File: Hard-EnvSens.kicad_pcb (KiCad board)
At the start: 2 copper layers, 54 parts, among them Q1 SS8050, Q2 SS8050, U1 LD1117S33TR_SOT223, U2 ESP32-C6-WROOM-1, U3 CP2104, U4 VEML7700-TR, U5 DPS368, U6 SGP41-D-R4, U7 SHT40-AD1B-R2

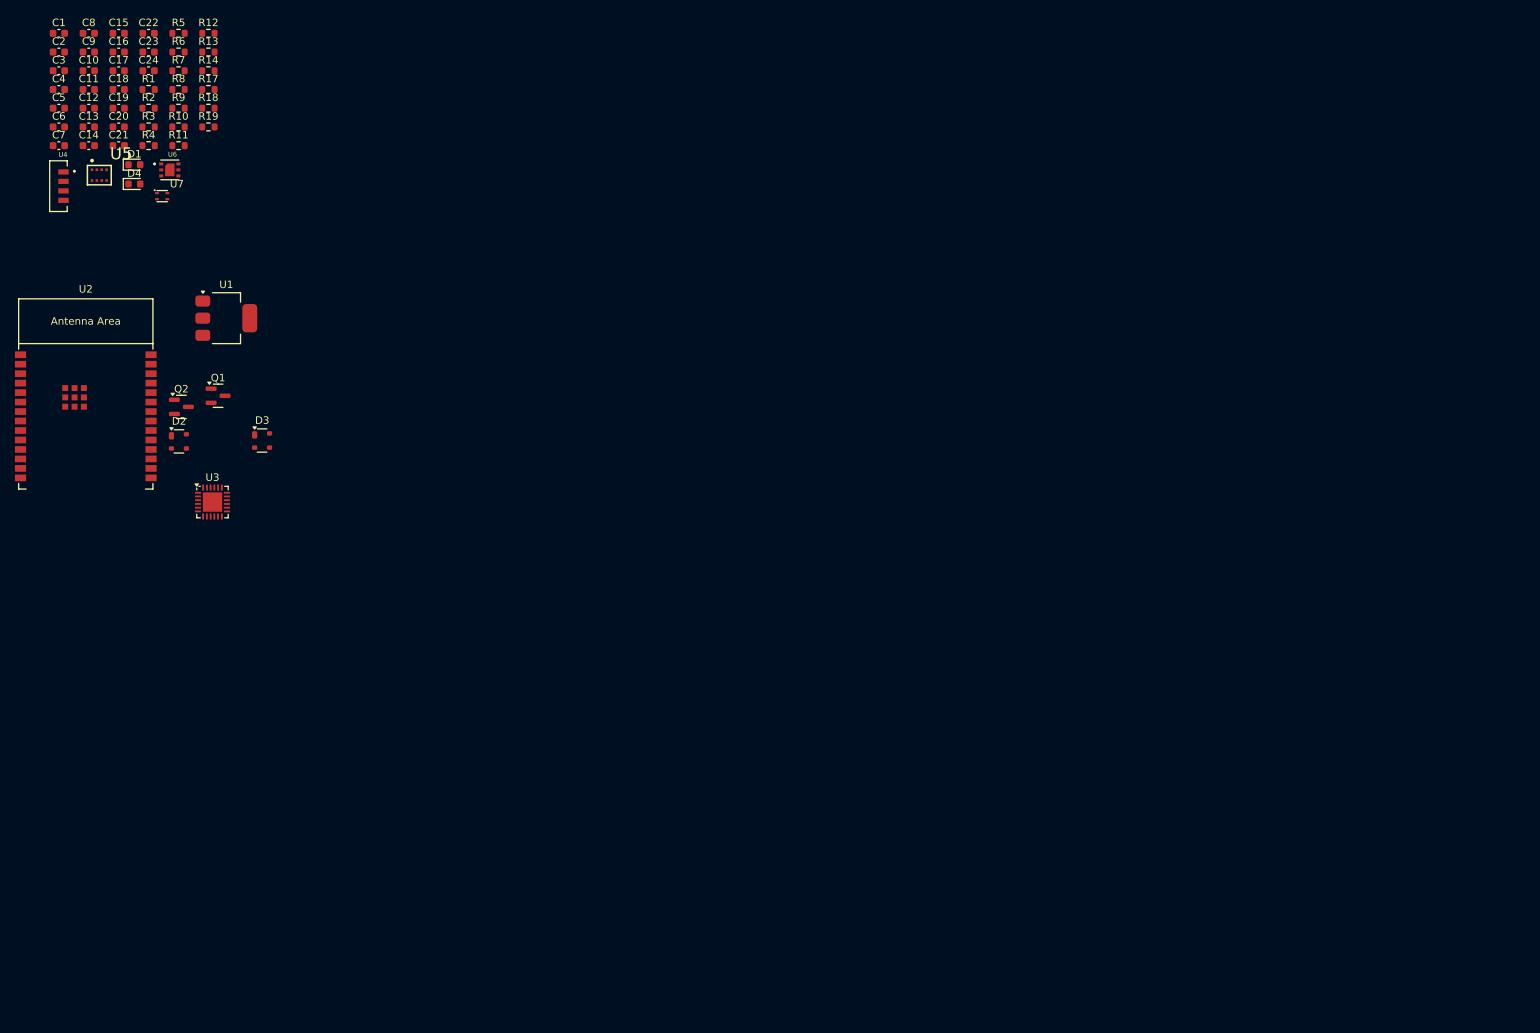
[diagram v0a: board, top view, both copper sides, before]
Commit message: Schematic done, Bottom board
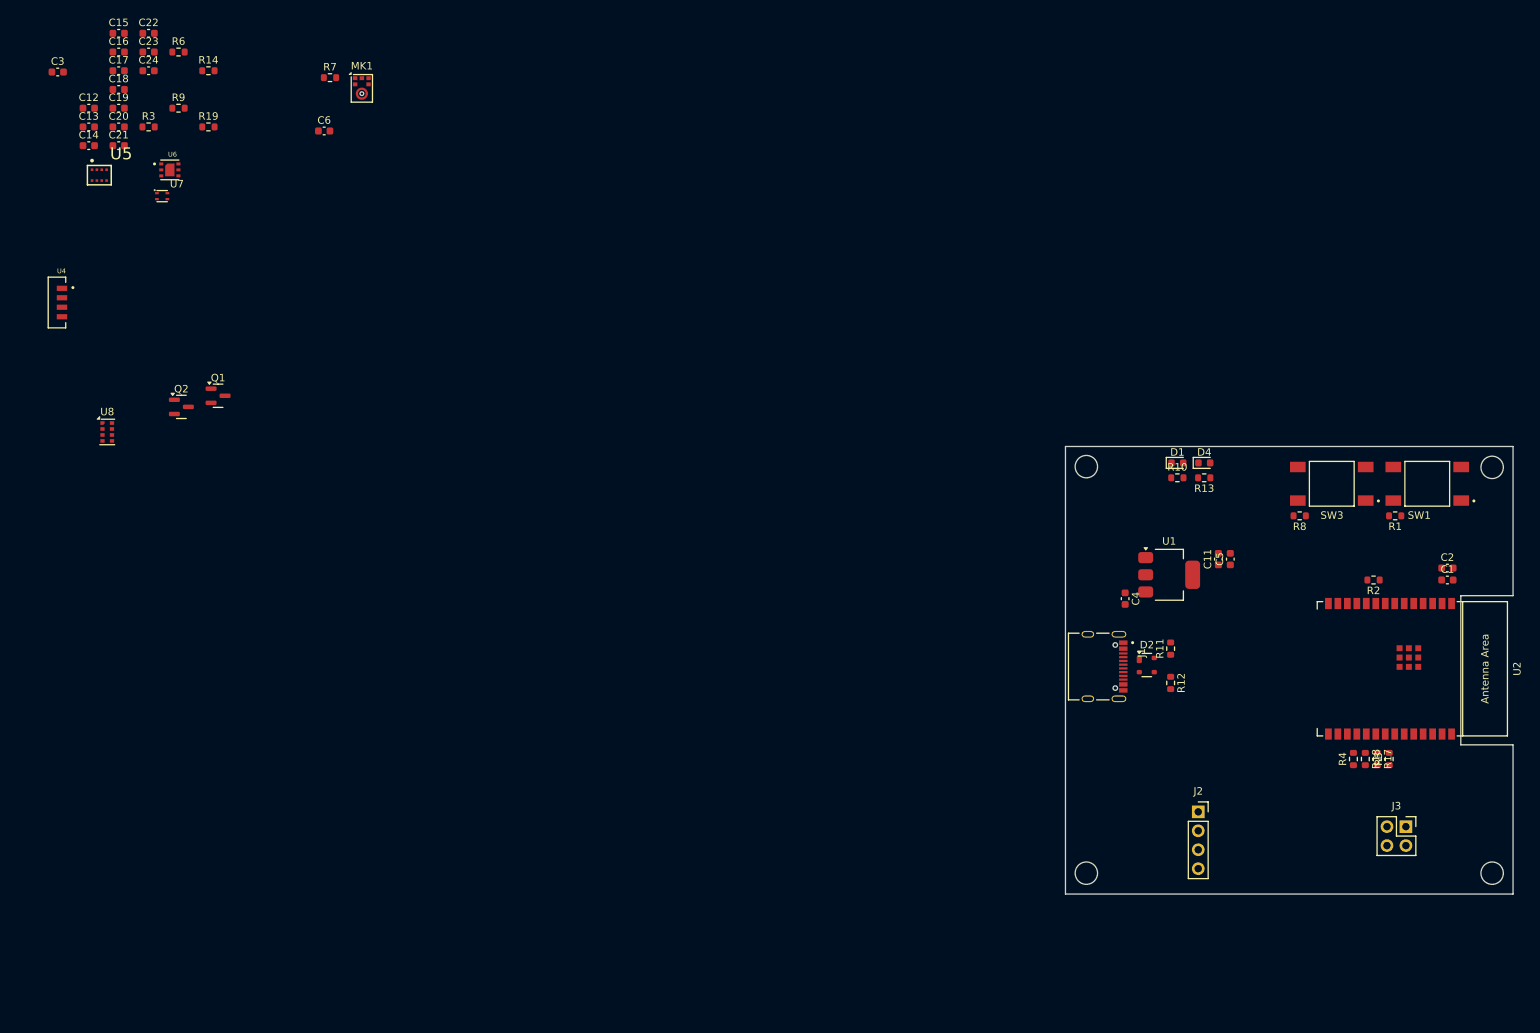
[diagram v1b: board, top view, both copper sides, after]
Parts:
- removed C10: 4.7k, Capacitor_SMD:C_0603_1608Metric
- removed C7, C8: 100nF, Capacitor_SMD:C_0603_1608Metric
- removed C9: 10uF, Capacitor_SMD:C_0603_1608Metric
- removed D3: SP0503BAHT, Package_TO_SOT_SMD:SOT-143
- removed U3: CP2104, Package_DFN_QFN:QFN-24-1EP_4x4mm_P0.5mm_EP2.6x2.6mm
- added J1: TYPE-C-31-M-12, Biblioteca_Kicad:HRO_TYPE-C-31-M-12, F.Cu at (103.1, 79.7)
- added J2: Conn_01x04_Socket, Connector_PinSocket_2.54mm:PinSocket_1x04_P2.54mm_Vertical, F.Cu at (117.9, 99.2)
- added J3: Conn_02x02_Odd_Even, Connector_PinSocket_2.54mm:PinSocket_2x02_P2.54mm_Vertical, F.Cu at (145.7, 101.2)
- added MK1: ICS-43434, Sensor_Audio:InvenSense_ICS-43434-6_3.5x2.65mm, F.Cu at (5.78, 2.19)
- added SW1: SW_Push, Biblioteca_Kicad:SW_3-1437565-0, F.Cu at (148.6, 55.2)
- added SW3: SW_Push, Biblioteca_Kicad:SW_3-1437565-0, F.Cu at (135.8, 55.2)
- added U8: AS7341-DLGT, Package_LGA:AMS_OLGA-8_2x3.1mm_P0.8mm, F.Cu at (-28.4, 48.3)
- C6: value 10uF -> 4.7uF
- R11, R12: value 100R -> 5.11k
- R7: value 4.7k -> 100K
- moved C1 200.1 mm to (151.3, 68.1)
- moved C2 198.6 mm to (151.3, 66.5)
- moved R5 189.2 mm to (143.5, 92.1), turned to 90 degrees
- moved R4 181.2 mm to (138.7, 92.1), turned to 90 degrees
- moved R17 180.6 mm to (141.9, 92.1), turned to -90 degrees
- moved U2 178.1 mm to (143.6, 80.0), turned to -90 degrees
- moved R18 178.0 mm to (140.3, 92.1), turned to -90 degrees
- moved R1 176.6 mm to (144.3, 59.5), turned to 180 degrees
- moved R2 176.0 mm to (141.4, 68.1), turned to 180 degrees
- moved C5 168.3 mm to (122.2, 65.3), turned to 90 degrees
- moved C11 164.0 mm to (120.6, 65.3), turned to 90 degrees
- moved R8 160.8 mm to (131.5, 59.5), turned to 180 degrees
- moved C4 158.4 mm to (108.1, 70.6), turned to -90 degrees
- moved R12 155.6 mm to (114.2, 81.9), turned to -90 degrees
- moved R11 149.1 mm to (114.2, 77.3), turned to 90 degrees
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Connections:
- C20 pad 1: +5V -> +3V3
- D2 pad 2: Net-(P1-D+) -> D+
- D2 pad 3: Net-(P1-D-) -> D-
- R11 pad 2: TX -> GND
- R12 pad 2: RX -> GND
- R7 pad 1: Net-(U3-~{RST}) -> GND
- R7 pad 2: +3V3 -> SD
- U2 pad 5: unconnected-(U2-MTDI/GPIO5/ADC1_CH5-Pad5) -> SD
- U2 pad 6: unconnected-(U2-MTCK/GPIO6/ADC1_CH6-Pad6) -> SCK
- U2 pad 7: unconnected-(U2-MTDO/GPIO7-Pad7) -> WS
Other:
- board outline added: 60 x 60 mm

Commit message: Started connections and sensors pcb
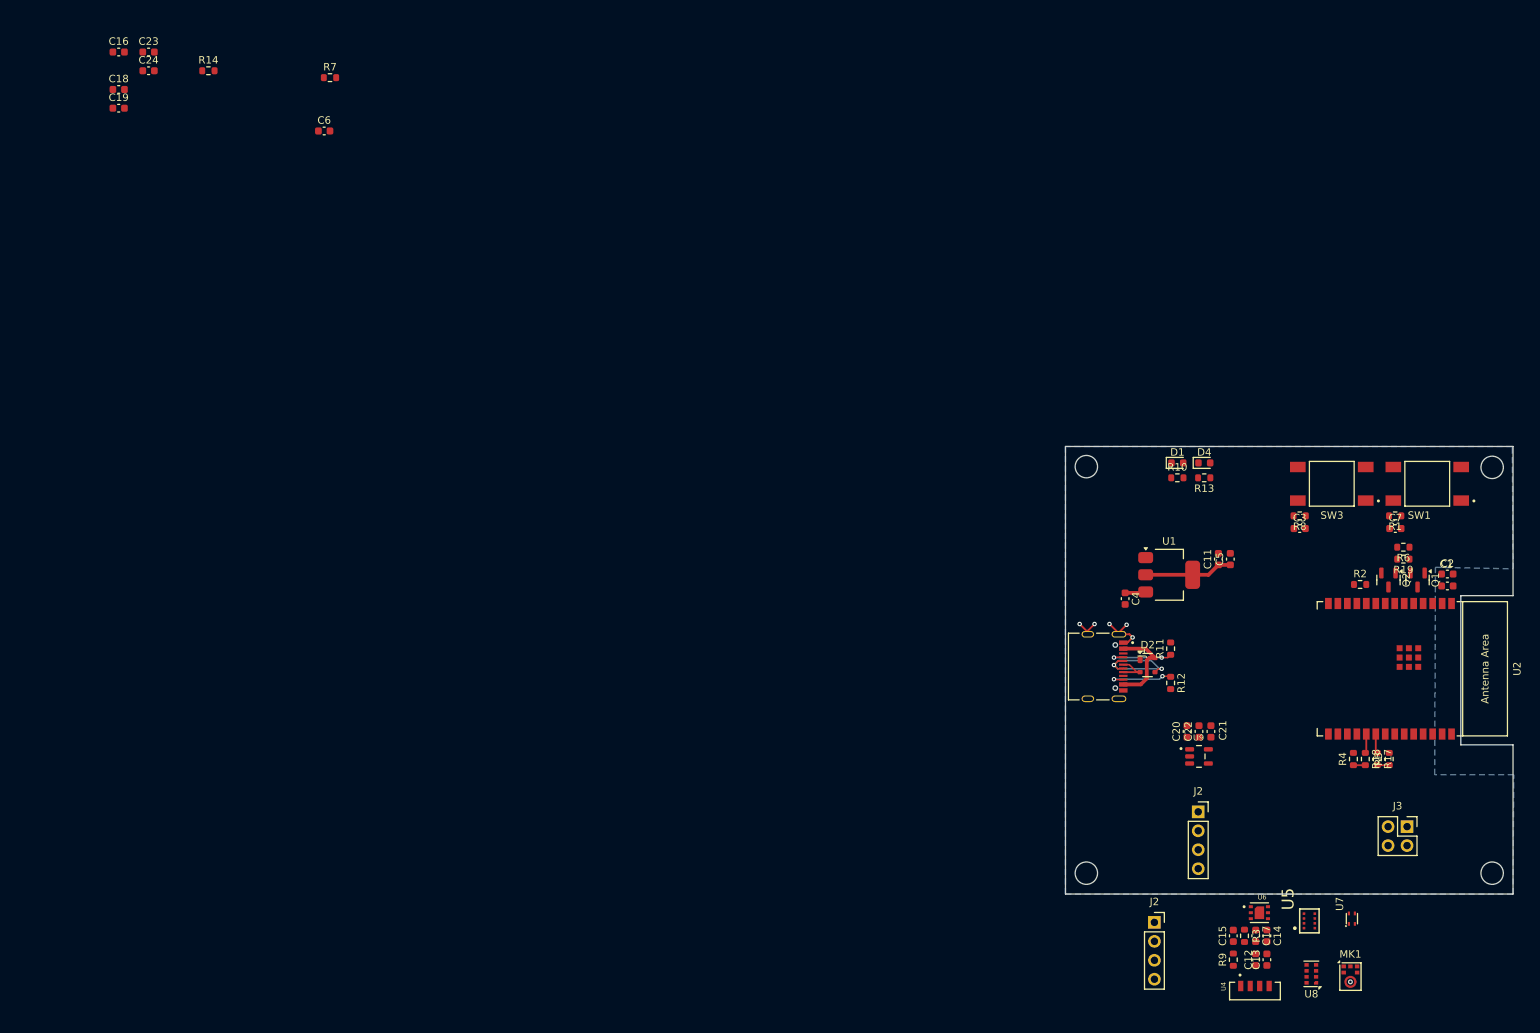
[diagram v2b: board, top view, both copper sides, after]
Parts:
- added C7: 1uF, Capacitor_SMD:C_0603_1608Metric, F.Cu at (144.3, 61.2)
- added J2: Conn_01x04_Socket, Connector_PinSocket_2.54mm:PinSocket_1x04_P2.54mm_Vertical, F.Cu at (112.0, 114.0)
- added U9: TPS79318DBVTG4, libs:SOT95P280X145-5N, F.Cu at (118.0, 91.8)
- moved C12 193.7 mm to (125.6, 119.0), turned to 90 degrees
- moved C13 193.4 mm to (127.1, 119.0), turned to 90 degrees
- moved C15 192.3 mm to (122.6, 115.8), turned to 90 degrees
- moved C17 191.5 mm to (125.6, 115.8), turned to -90 degrees
- moved U5 190.6 mm to (132.8, 113.8), turned to 90 degrees
- moved C14 190.2 mm to (127.1, 115.8), turned to -90 degrees
- moved U7 186.6 mm to (138.5, 113.5), turned to 90 degrees
- moved U4 185.2 mm to (125.5, 123.2), turned to 90 degrees
- moved R3 182.6 mm to (124.1, 115.8), turned to -90 degrees
- moved R9 181.7 mm to (122.6, 119.0), turned to 90 degrees
- moved MK1 178.2 mm to (138.3, 121.3)
- moved C3 177.4 mm to (131.5, 61.2)
- moved R6 177.1 mm to (145.4, 63.7), turned to 180 degrees
- moved U8 177.0 mm to (133.1, 120.9), turned to 180 degrees
- moved U6 176.8 mm to (126.1, 112.7)
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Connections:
- U2 pad 15: IO9 -> unconnected-(U2-GPIO9-Pad15)
- U2 pad 4: unconnected-(U2-MTMS/GPIO4/ADC1_CH4-Pad4) -> IO9
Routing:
- net D-: track 0.00 -> 17.8 mm, vias 0 -> 2
- net +5V: track 0.00 -> 14.7 mm
- net +3V3: track 0.00 -> 11.9 mm
- net GND: track 0.00 -> 10.7 mm, vias 0 -> 5
- net Net-(J1-CC2): track 0.00 -> 9.07 mm, vias 0 -> 2
- net Net-(J1-CC1): track 0.00 -> 9.03 mm, vias 0 -> 2
- net D+: track 0.00 -> 5.04 mm
- net Net-(U2-GPIO22): track 0.00 -> 2.61 mm
- net Net-(U2-GPIO21): track 0.00 -> 2.58 mm
- net Sda: track 0.00 -> 1.60 mm
- net Scl: track 0.00 -> 1.60 mm
- added copper zone on B.Cu, net GND

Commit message: Full connected board, no charger
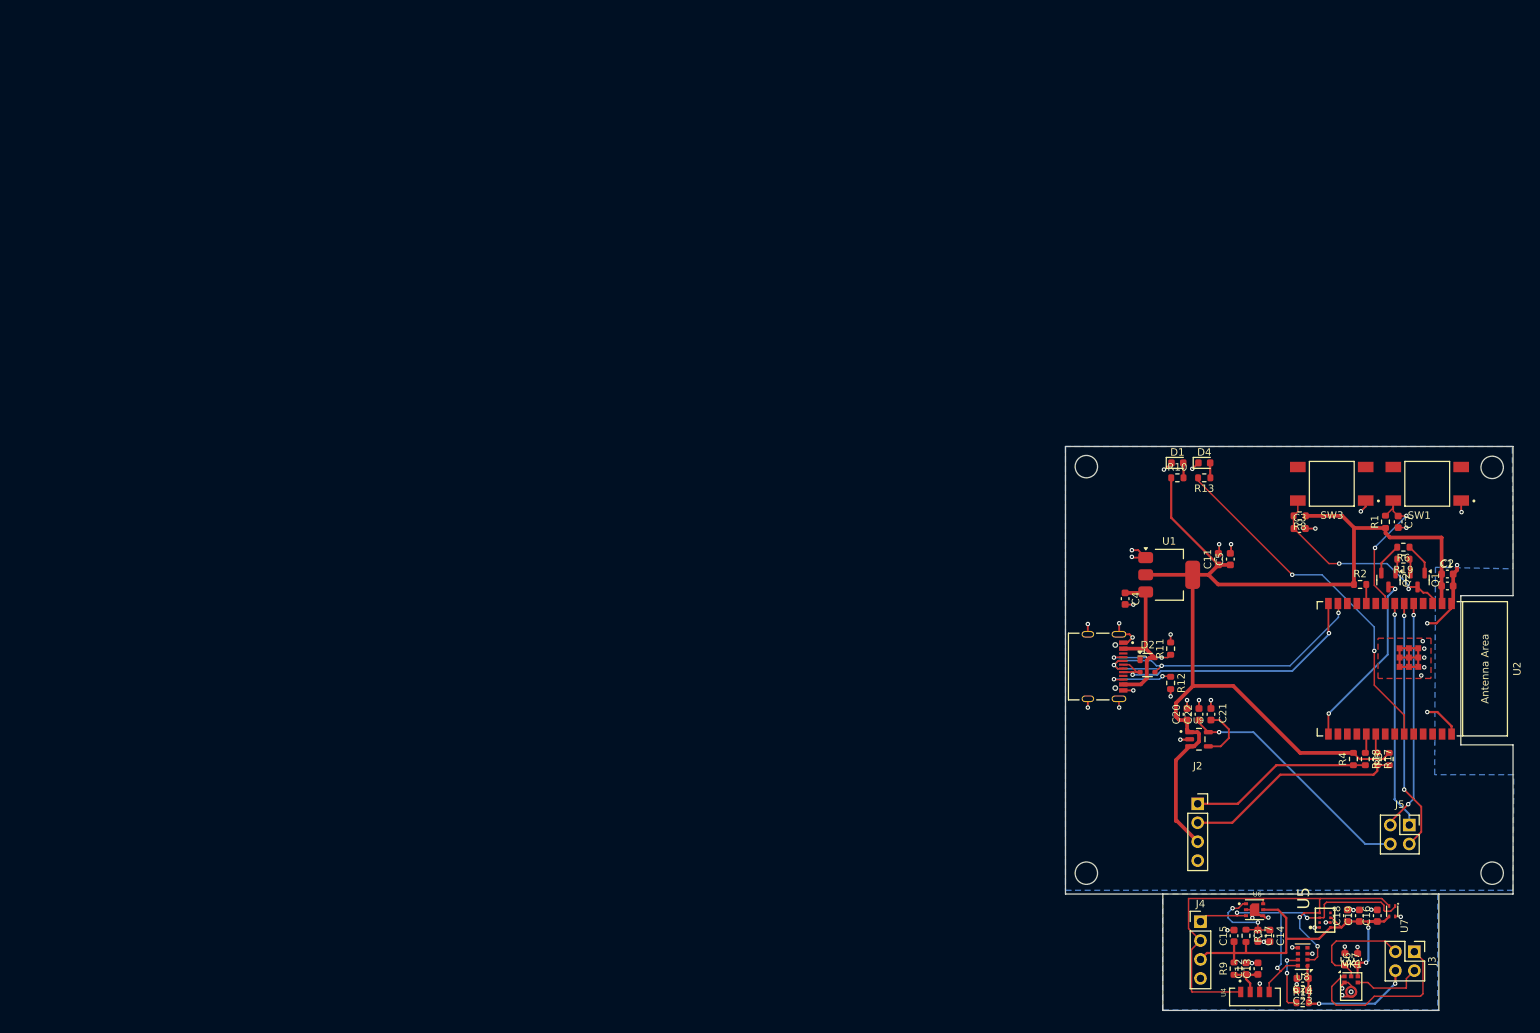
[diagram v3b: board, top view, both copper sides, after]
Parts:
- removed the J2 at (112.0, 114.0)
- added J4: Conn_01x04_Pin, Connector_PinHeader_2.54mm:PinHeader_1x04_P2.54mm_Vertical, F.Cu at (118.2, 113.9)
- added J5: Conn_02x02_Odd_Even, Connector_PinSocket_2.54mm:PinSocket_2x02_P2.54mm_Vertical, F.Cu at (146.2, 101.0)
- C12: value C_Small -> 100nF
- C13: value C_Small -> 10uF
- J3: footprint Connector_PinSocket_2.54mm:PinSocket_2x02_P2.54mm_Vertical -> Connector_PinHeader_2.54mm:PinHeader_2x02_P2.54mm_Vertical
- moved C16 204.6 mm to (141.9, 113.1), turned to 90 degrees
- moved C23 199.4 mm to (131.9, 123.1), turned to 180 degrees
- moved C18 198.5 mm to (137.9, 113.1), turned to 90 degrees
- moved C19 198.4 mm to (139.5, 113.1), turned to 90 degrees
- moved C24 196.8 mm to (131.9, 121.5), turned to 180 degrees
- moved R14 192.7 mm to (131.9, 124.8)
- moved R7 180.2 mm to (137.6, 119.0), turned to -90 degrees
- moved C6 177.6 mm to (139.3, 119.0), turned to 90 degrees
- moved J3 16.8 mm to (146.9, 117.9), turned to -90 degrees
- moved U7 5.49 mm to (143.9, 112.5), turned to -90 degrees
- moved U8 2.58 mm to (131.9, 118.6)
- moved C20 2.30 mm to (116.4, 86.1)
- moved C21 2.30 mm to (119.6, 86.1)
- moved C22 2.30 mm to (118.0, 86.1)
- moved U9 2.30 mm to (118.0, 89.5)
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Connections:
- C12 pad 2: GND -> GND2
- C13 pad 2: GND -> GND2
- C14 pad 2: GND -> GND2
- C15 pad 1: +3V3 -> +3V3top
- C15 pad 2: GND -> GND2
- C16 pad 1: +3V3 -> +3V3top
- C16 pad 2: GND -> GND2
- C17 pad 2: GND -> GND2
- C18 pad 1: +3V3 -> +3V3top
- C18 pad 2: GND -> GND2
- C19 pad 1: +3V3 -> +3V3top
- C19 pad 2: GND -> GND2
- C23 pad 1: +1V8 -> +1V8top
- C23 pad 2: GND -> GND2
- C24 pad 1: +1V8 -> +1V8top
- C24 pad 2: GND -> GND2
- C6 pad 1: +3V3 -> +3V3top
- C6 pad 2: GND -> GND2
- J3 pad 1: WS -> WStop
- J3 pad 2: SCK -> SCKtop
- J3 pad 3: SD -> SDtop
- J3 pad 4: +1V8 -> +1V8top
- MK1 pad 1: WS -> WStop
- MK1 pad 2: GND -> GND2
- MK1 pad 3: GND -> GND2
- MK1 pad 4: SCK -> SCKtop
- MK1 pad 5: +3V3 -> +3V3top
- MK1 pad 6: SD -> SDtop
- R14 pad 2: +1V8 -> +1V8top
- R3 pad 2: +3V3 -> +3V3top
- R7 pad 1: GND -> GND2
- R7 pad 2: SD -> SDtop
- R9 pad 2: +3V3 -> +3V3top
- U2 pad 15: unconnected-(U2-GPIO9-Pad15) -> IO9
- U2 pad 4: IO9 -> unconnected-(U2-MTMS/GPIO4/ADC1_CH4-Pad4)
- U4 pad 1: Scl -> Scltop
- U4 pad 3: GND -> GND2
- U4 pad 4: Sda -> Sdatop
- U5 pad 1: GND -> GND2
- U5 pad 3: Sda -> Sdatop
- U5 pad 4: Scl -> Scltop
- U5 pad 6: +3V3 -> +3V3top
- U5 pad 7: GND -> GND2
- U5 pad 8: +3V3 -> +3V3top
- U6 pad 2: GND -> GND2
- U6 pad 3: Sda -> Sdatop
- U6 pad 4: GND -> GND2
- U6 pad 5: +3V3 -> +3V3top
- U6 pad 6: Scl -> Scltop
- U6 pad 7: GND -> GND2
- U7 pad 1: Sda -> Sdatop
- U7 pad 2: Scl -> Scltop
- U7 pad 3: +3V3 -> +3V3top
- U7 pad 4: GND -> GND2
- U8 pad 1: +1V8 -> +1V8top
- U8 pad 2: Scl -> Scltop
- U8 pad 3: GND -> GND2
- U8 pad 5: GND -> GND2
- U8 pad 8: Sda -> Sdatop
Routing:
- net +3V3: track 11.9 -> 155.4 mm
- net Scltop: track 0.00 -> 61.0 mm, vias 0 -> 2
- net GND: track 10.7 -> 63.7 mm, vias 5 -> 31
- net +3V3top: track 0.00 -> 51.2 mm, vias 0 -> 2
- net Net-(U2-GPIO15): track 0.00 -> 48.1 mm, vias 0 -> 2
- net Sdatop: track 0.00 -> 46.2 mm, vias 0 -> 3
- net SCK: track 0.00 -> 34.1 mm, vias 0 -> 2
- net D+: track 5.04 -> 38.1 mm, vias 0 -> 2
- net +1V8: track 0.00 -> 32.7 mm, vias 0 -> 1
- net SD: track 0.00 -> 31.0 mm, vias 0 -> 2
- net WS: track 0.00 -> 30.5 mm, vias 0 -> 1
- net D-: track 17.8 -> 46.3 mm, vias 2 -> 3
- net EN: track 0.00 -> 27.8 mm, vias 0 -> 2
- net Scl: track 1.60 -> 29.3 mm
- net GND2: track 0.00 -> 24.7 mm, vias 0 -> 18
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- added copper zone on F.Cu, net GND
- added copper zone on B.Cu, net GND2
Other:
- board size 60 x 60 mm -> 60 x 75.6 mm
